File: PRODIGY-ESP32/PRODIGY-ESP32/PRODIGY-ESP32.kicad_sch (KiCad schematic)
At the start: 27 parts, among them J1 Bus_M.2_Socket_B, Q1 BC850, Q2 BC850, SW1 SW_Push, U1 ESP32-S3-WROOM-1, U2 FT231XQ, U3 TS3USB221AQRSERQ1

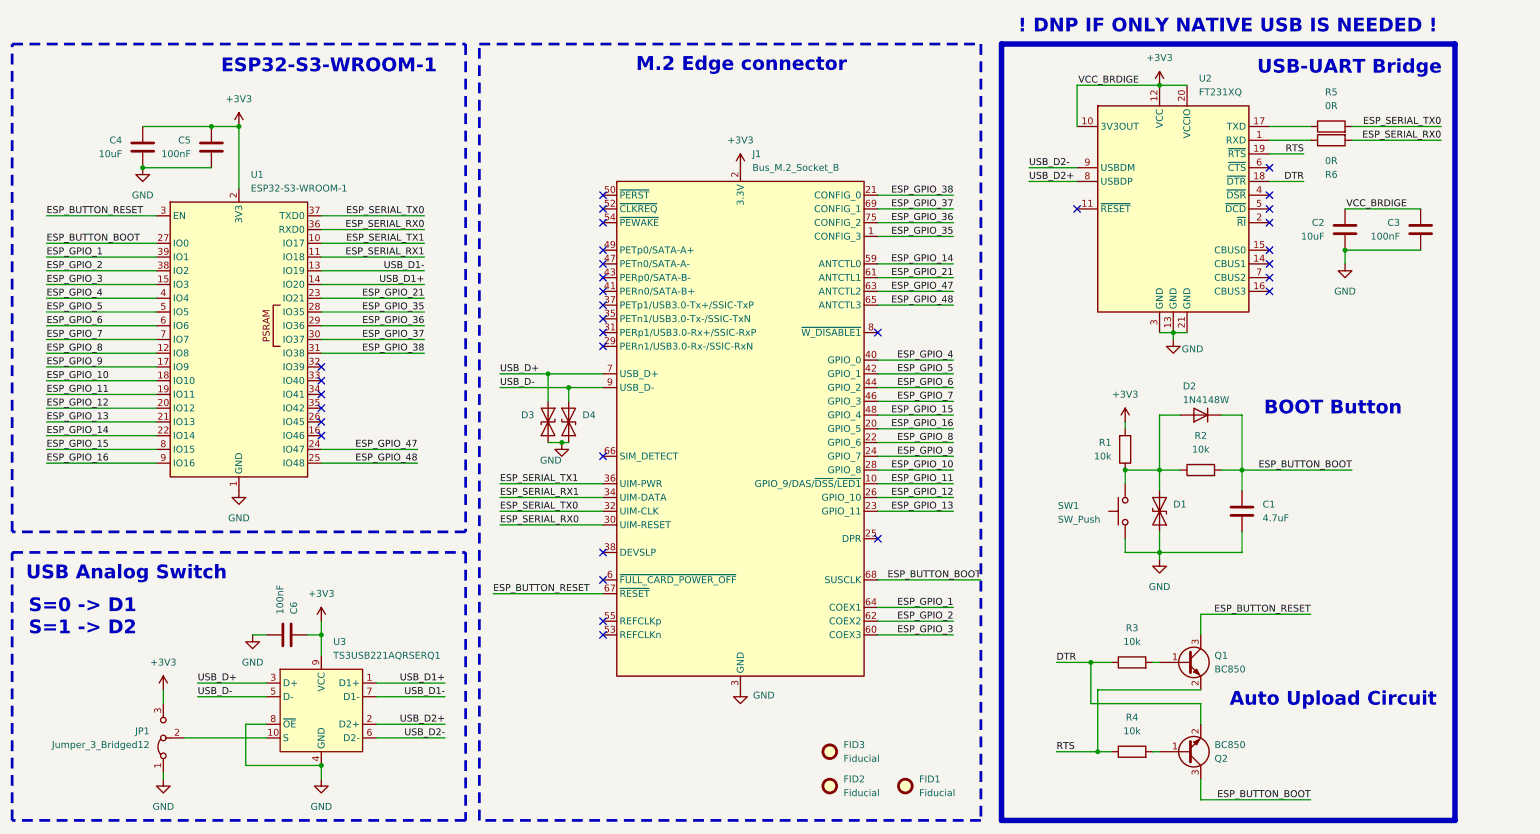
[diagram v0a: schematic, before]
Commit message: All footprint assosiations have been made across all schematics.
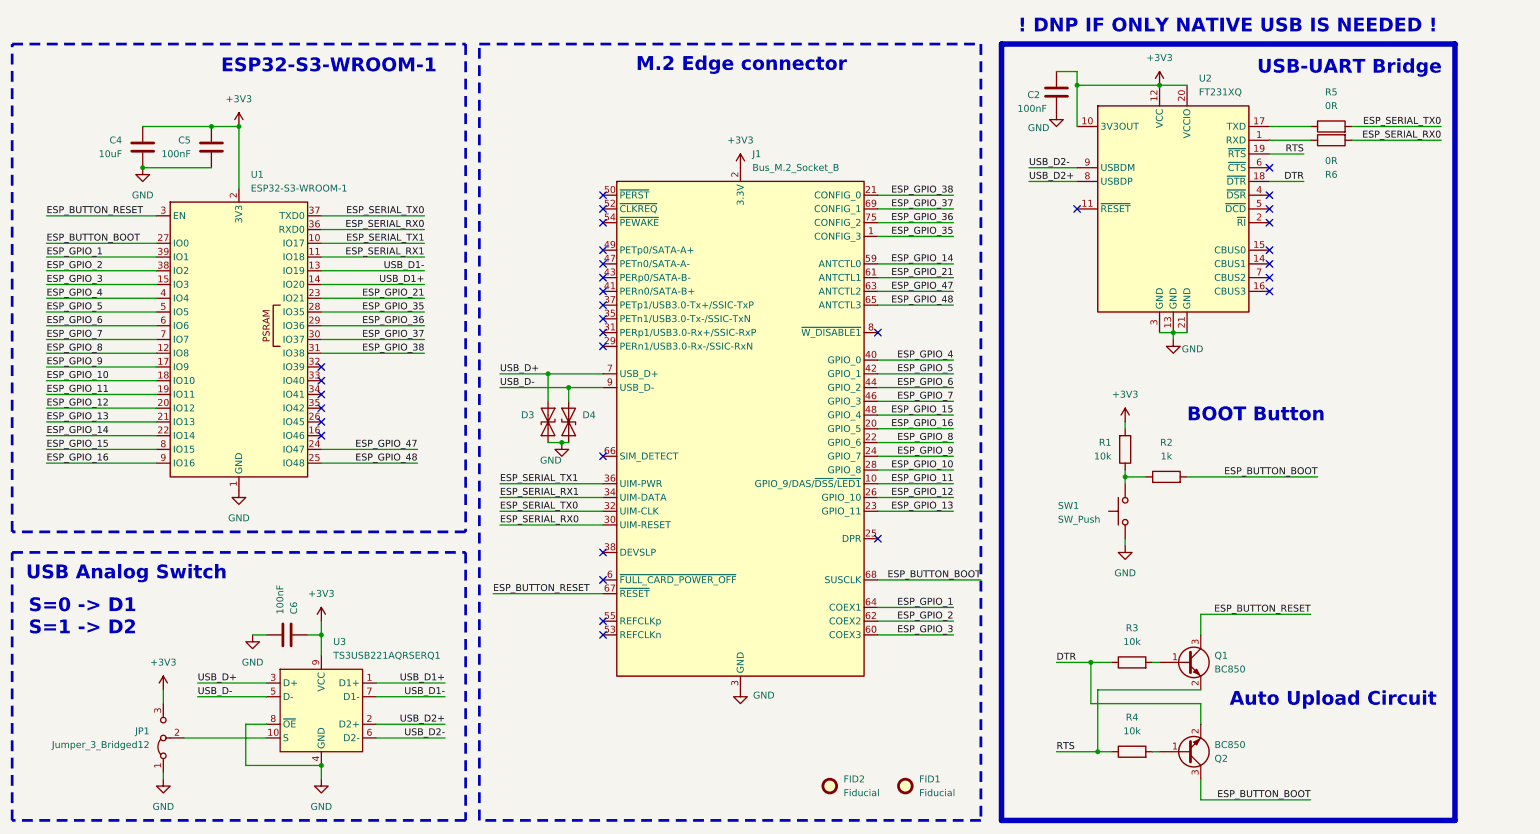
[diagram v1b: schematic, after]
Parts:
- removed C1: 4.7uF, symbol Device:C
- removed C3: 100nF, symbol Device:C
- removed D1: SD05_SOD323, Diode_SMD:D_SOD-323, symbol Diode:SD05_SOD323
- removed D2: 1N4148W, Diode_SMD:D_SOD-123, symbol Diode:1N4148W
- removed FID3: Fiducial, symbol Mechanical:Fiducial
- C2: value 10uF -> 100nF; footprint (none) -> Capacitor_SMD:C_0603_1608Metric
- C4: footprint (none) -> Capacitor_SMD:C_0805_2012Metric
- C5, C6: footprint (none) -> Capacitor_SMD:C_0603_1608Metric
- FID1, FID2: footprint (none) -> Fiducial:Fiducial_0.5mm_Mask1.5mm
- JP1: footprint (none) -> Jumper:SolderJumper-3_P1.3mm_Open_Pad1.0x1.5mm
- R2: value 10k -> 1k
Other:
- moved on the sheet: R2

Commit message: ESP32 and ATMEGA bom done.
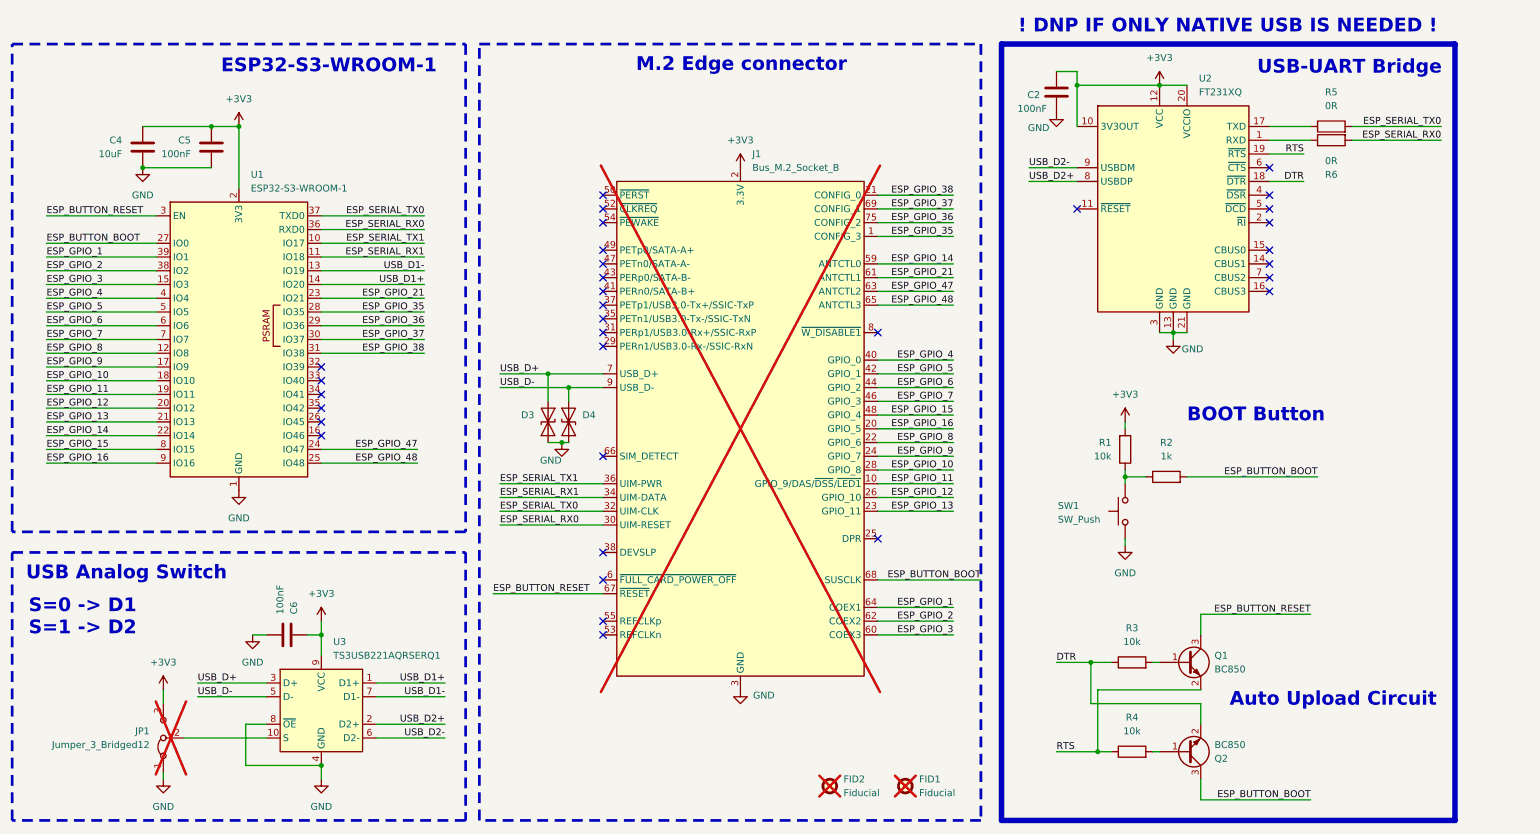
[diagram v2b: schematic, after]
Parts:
- C2, C5, C6: TME (none) -> CL10B104KB8NNNC
- C4: TME (none) -> CL21A106KOQNNNE
- D3, D4: TME (none) -> SD05.TCT
- FID1, FID2, J1, JP1: now not fitted
- Q1, Q2: TME (none) -> BC850B-DIO
- R1, R3, R4: TME (none) -> WR06X1002FTL
- R2: TME (none) -> RC0603JR-071K
- R5, R6: TME (none) -> SMD0603-0R
- SW1: TME (none) -> KMR231GLFS
- U1: TME (none) -> ESP32S3-WRM1-16R8
- U2: TME (none) -> FT231XQ-R
- U3: footprint Package_DFN_QFN:UQFN-10_1.4x1.8mm_P0.4mm -> Package_DFN_QFN:Texas_UQFN-10_1.5x2mm_P0.5mm; MOUSER (none) -> 595-S3USB221AQRSERQ1

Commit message: Shcematic fixes to ESP32
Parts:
- removed U3: TS3USB221AQRSERQ1, Package_DFN_QFN:Texas_UQFN-10_1.5x2mm_P0.5mm, symbol Interface_USB:TS3USB30ERSWR
- added U2: TS3USB221AQRSERQ1, Package_DFN_QFN:Texas_UQFN-10_1.5x2mm_P0.5mm, symbol TS3USB221AQRSERQ1:TS3USB221AQRSERQ1
- renumbered C4 to C1, C5 to C2, C6 to C3, C2 to C4, D3 to D1, D4 to D2, FID2 to FID1, FID1 to FID2, R3 to R2, R4 to R3, R2 to R4, U2 to U3
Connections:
- net +3V3: now also JP1.1 (A), U2.10 (VCC); no longer JP1.3 (B)
- net GND: now also JP1.3 (B), U2.5 (GND), U2.6 (~{OE}); no longer JP1.1 (A)
- net USB_D+: now also U2.8 (D+)
- net USB_D-: now also U2.7 (D-)
- net USB_D1+: now also U3.8 (USBDP), U2.1 (D1+); no longer U1.14 (IO20)
- net USB_D1-: now also U3.9 (USBDM), U2.2 (D1-); no longer U1.13 (IO19)
- net USB_D2+: now also U1.14 (IO20), U2.3 (D2+); no longer U3.8 (USBDP)
- net USB_D2-: now also U1.13 (IO19), U2.4 (D2-); no longer U3.9 (USBDM)
- net at JP1.2 (C): now also U2.9 (S)
